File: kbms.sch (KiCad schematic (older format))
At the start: 4 parts

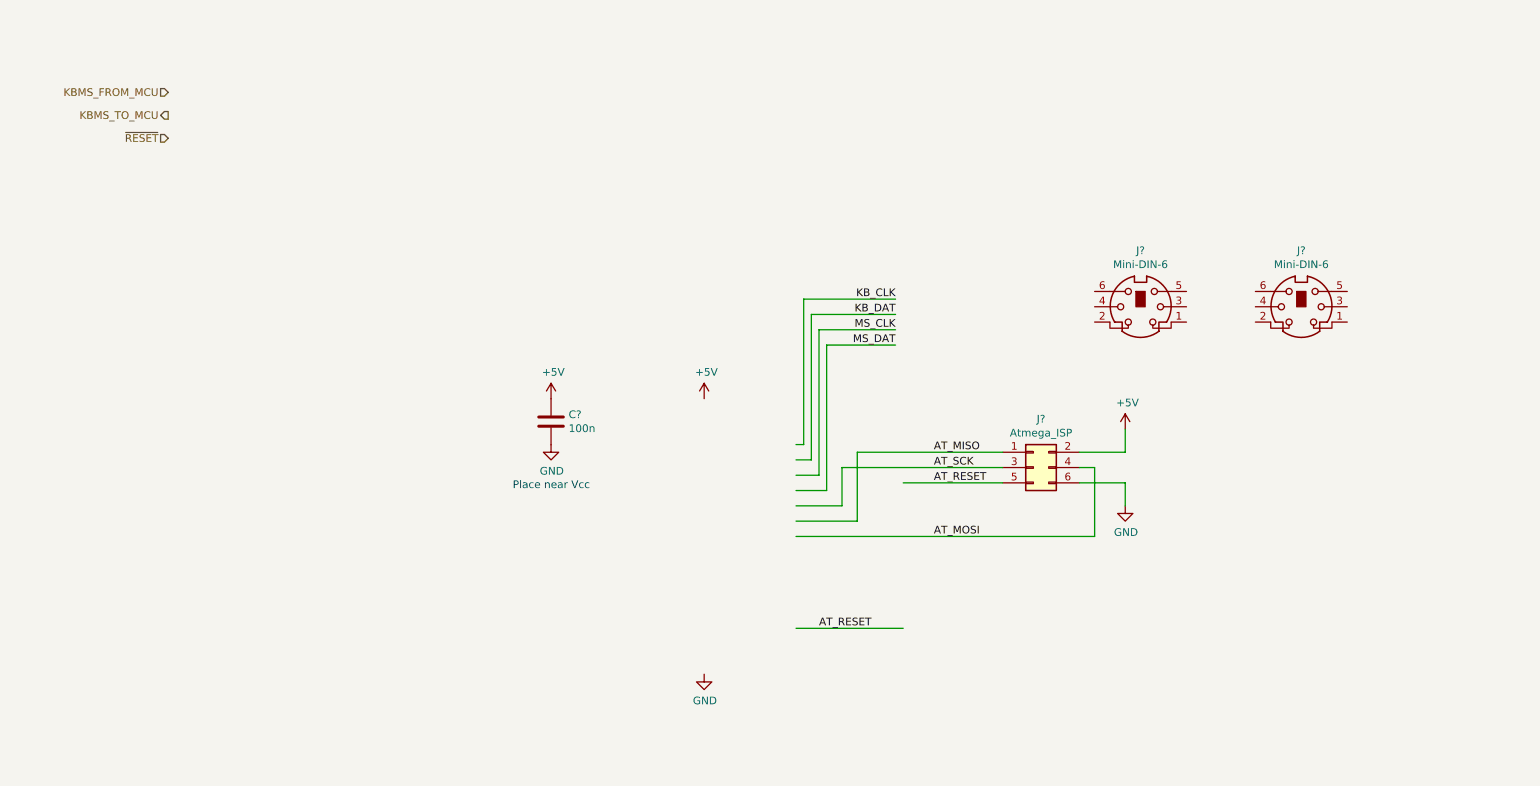
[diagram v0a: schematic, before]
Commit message: Added some footprints. Basic board outline.
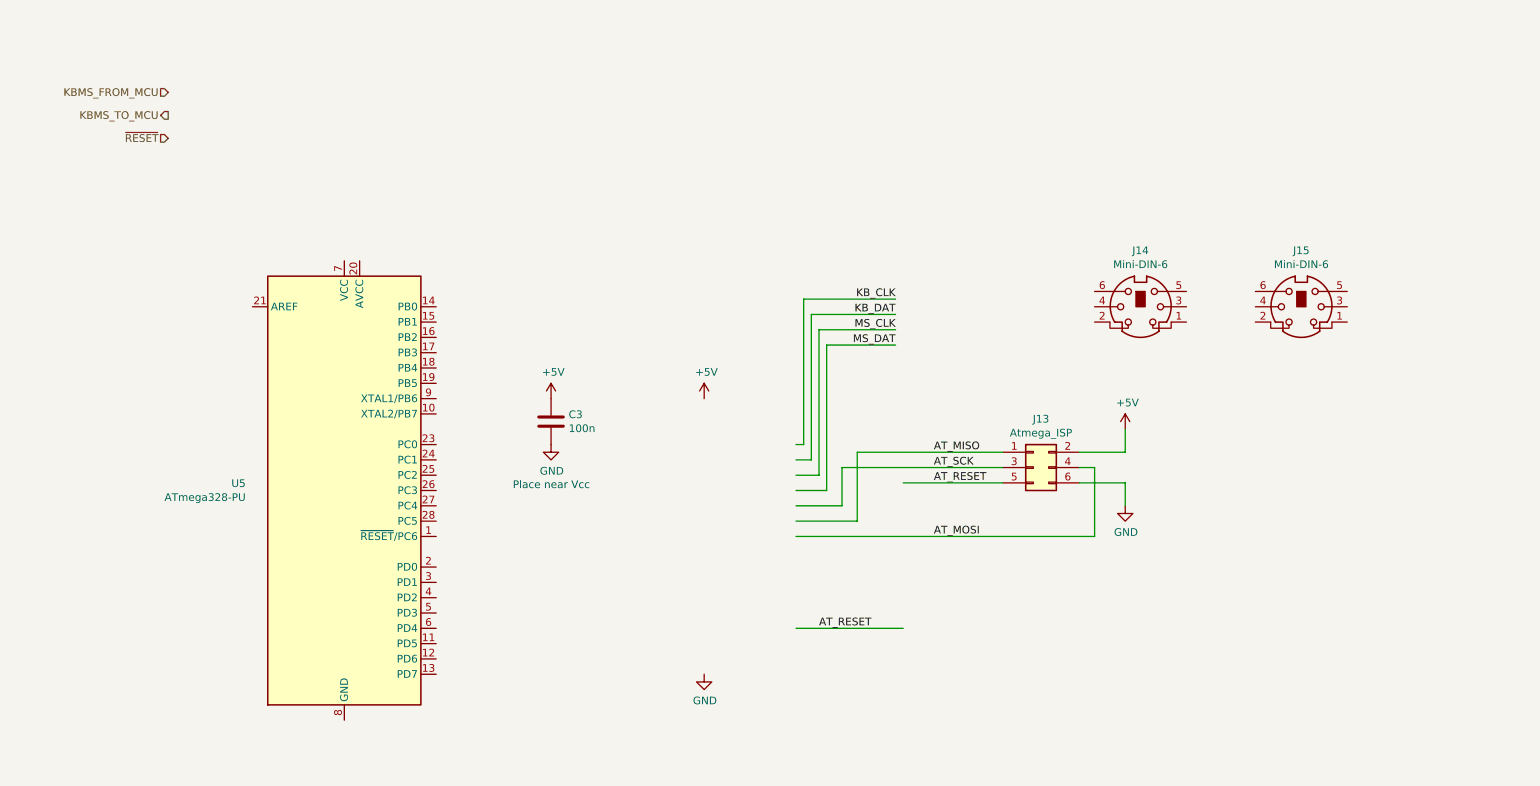
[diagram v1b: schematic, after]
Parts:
- added U5: ATmega328-PU, Package_DIP:DIP-28_W7.62mm, symbol MCU_Microchip_ATmega:ATmega328-PU
- C3: renamed from C?; footprint (none) -> Capacitor_THT:C_Disc_D5.0mm_W2.5mm_P2.50mm
- J13: renamed from J?; footprint (none) -> Connector_PinHeader_2.54mm:PinHeader_2x03_P2.54mm_Vertical
- J14, J15: renamed from J?; footprint (none) -> JGP Footprints:mini-DIN 6
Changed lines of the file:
@@
 $Descr A4 11693 8268
 encoding utf-8
-Sheet 11 11
+Sheet 9 11
 Title "Neotron 32K"
 Date "2019-12-08"
@@
 P 7350 3650
 AR Path="/5DF43D9A" Ref="J?"  Part="1"
-AR Path="/5DF2662E/5DF43D9A" Ref="J?"  Part="1"
-F 0 "J?" H 7400 3967 50  0000 C CNN
+AR Path="/5DF2662E/5DF43D9A" Ref="J13"  Part="1"
+F 0 "J13" H 7400 3967 50  0000 C CNN
 F 1 "Atmega_ISP" H 7400 3876 50  0000 C CNN
-F 2 "" H 7350 3650 50  0001 C CNN
+F 2 "Connector_PinHeader_2.54mm:PinHeader_2x03_P2.54mm_Vertical" H 7350 3650 50  0001 C CNN
 F 3 "~" H 7350 3650 50  0001 C CNN
 	1    7350 3650
@@
 P 7950 3400
 AR Path="/5DF43DA0" Ref="#PWR?"  Part="1"
-AR Path="/5DF2662E/5DF43DA0" Ref="#PWR0105"  Part="1"
-F 0 "#PWR0105" H 7950 3250 50  0001 C CNN
+AR Path="/5DF2662E/5DF43DA0" Ref="#PWR018"  Part="1"
+F 0 "#PWR018" H 7950 3250 50  0001 C CNN
 F 1 "+5V" H 7965 3573 50  0000 C CNN
 F 2 "" H 7950 3400 50  0001 C CNN
@@
 P 7950 3900
 AR Path="/5DF43DA6" Ref="#PWR?"  Part="1"
-AR Path="/5DF2662E/5DF43DA6" Ref="#PWR0106"  Part="1"
-F 0 "#PWR0106" H 7950 3650 50  0001 C CNN
+AR Path="/5DF2662E/5DF43DA6" Ref="#PWR019"  Part="1"
+F 0 "#PWR019" H 7950 3650 50  0001 C CNN
 F 1 "GND" H 7955 3727 50  0000 C CNN
 F 2 "" H 7950 3900 50  0001 C CNN
@@
 P 5200 3200
 AR Path="/5DF43DBB" Ref="#PWR?"  Part="1"
-AR Path="/5DF2662E/5DF43DBB" Ref="#PWR0107"  Part="1"
-F 0 "#PWR0107" H 5200 3050 50  0001 C CNN
+AR Path="/5DF2662E/5DF43DBB" Ref="#PWR016"  Part="1"
+F 0 "#PWR016" H 5200 3050 50  0001 C CNN
 F 1 "+5V" H 5215 3373 50  0000 C CNN
 F 2 "" H 5200 3200 50  0001 C CNN
@@
 P 5200 5000
 AR Path="/5DF43DC1" Ref="#PWR?"  Part="1"
-AR Path="/5DF2662E/5DF43DC1" Ref="#PWR0108"  Part="1"
-F 0 "#PWR0108" H 5200 4750 50  0001 C CNN
+AR Path="/5DF2662E/5DF43DC1" Ref="#PWR017"  Part="1"
+F 0 "#PWR017" H 5200 4750 50  0001 C CNN
 F 1 "GND" H 5205 4827 50  0000 C CNN
 F 2 "" H 5200 5000 50  0001 C CNN
@@
 P 4200 3350
 AR Path="/5DF43DC7" Ref="C?"  Part="1"
-AR Path="/5DF2662E/5DF43DC7" Ref="C?"  Part="1"
-F 0 "C?" H 4315 3396 50  0000 L CNN
+AR Path="/5DF2662E/5DF43DC7" Ref="C3"  Part="1"
+F 0 "C3" H 4315 3396 50  0000 L CNN
 F 1 "100n" H 4315 3305 50  0000 L CNN
-F 2 "" H 4238 3200 50  0001 C CNN
+F 2 "Capacitor_THT:C_Disc_D5.0mm_W2.5mm_P2.50mm" H 4238 3200 50  0001 C CNN
 F 3 "~" H 4200 3350 50  0001 C CNN
 	1    4200 3350
@@
 P 4200 3200
 AR Path="/5DF43DCD" Ref="#PWR?"  Part="1"
-AR Path="/5DF2662E/5DF43DCD" Ref="#PWR0109"  Part="1"
-F 0 "#PWR0109" H 4200 3050 50  0001 C CNN
+AR Path="/5DF2662E/5DF43DCD" Ref="#PWR014"  Part="1"
+F 0 "#PWR014" H 4200 3050 50  0001 C CNN
 F 1 "+5V" H 4215 3373 50  0000 C CNN
 F 2 "" H 4200 3200 50  0001 C CNN
@@
 P 4200 3500
 AR Path="/5DF43DD3" Ref="#PWR?"  Part="1"
-AR Path="/5DF2662E/5DF43DD3" Ref="#PWR0110"  Part="1"
-F 0 "#PWR0110" H 4200 3250 50  0001 C CNN
+AR Path="/5DF2662E/5DF43DD3" Ref="#PWR015"  Part="1"
+F 0 "#PWR015" H 4200 3250 50  0001 C CNN
 F 1 "GND" H 4205 3327 50  0000 C CNN
 F 2 "" H 4200 3500 50  0001 C CNN
@@
 P 8050 2600
 AR Path="/5DF4AE86" Ref="J?"  Part="1"
-AR Path="/5DF2662E/5DF4AE86" Ref="J?"  Part="1"
-F 0 "J?" H 8050 2967 50  0000 C CNN
+AR Path="/5DF2662E/5DF4AE86" Ref="J14"  Part="1"
+F 0 "J14" H 8050 2967 50  0000 C CNN
 F 1 "Mini-DIN-6" H 8050 2876 50  0000 C CNN
-F 2 "" H 8050 2600 50  0001 C CNN
+F 2 "JGP Footprints:mini-DIN 6" H 8050 2600 50  0001 C CNN
 F 3 "http://service.powerdynamics.com/ec/Catalog17/Section%2011.pdf" H 8050 2600 50  0001 C CNN
 	1    8050 2600
@@
 P 9100 2600
 AR Path="/5DF4AE8C" Ref="J?"  Part="1"
-AR Path="/5DF2662E/5DF4AE8C" Ref="J?"  Part="1"
-F 0 "J?" H 9100 2967 50  0000 C CNN
+AR Path="/5DF2662E/5DF4AE8C" Ref="J15"  Part="1"
+F 0 "J15" H 9100 2967 50  0000 C CNN
 F 1 "Mini-DIN-6" H 9100 2876 50  0000 C CNN
-F 2 "" H 9100 2600 50  0001 C CNN
+F 2 "JGP Footprints:mini-DIN 6" H 9100 2600 50  0001 C CNN
 F 3 "http://service.powerdynamics.com/ec/Catalog17/Section%2011.pdf" H 9100 2600 50  0001 C CNN
 	1    9100 2600
@@
 Text HLabel 1700 1500 0    50   Input ~ 0
 ~RESET
+$Comp
+L MCU_Microchip_ATmega:ATmega328-PU U5
+U 1 1 5E0F9E16
+P 2850 3800
+F 0 "U5" H 2206 3846 50  0000 R CNN
+F 1 "ATmega328-PU" H 2206 3755 50  0000 R CNN
+F 2 "Package_DIP:DIP-28_W7.62mm" H 2850 3800 50  0001 C CIN
+F 3 "http://ww1.microchip.com/downloads/en/DeviceDoc/ATmega328_P%20AVR%20MCU%20with%20picoPower%20Technology%20Data%20Sheet%2040001984A.pdf" H 2850 3800 50  0001 C CNN
+	1    2850 3800
+	1    0    0    -1
+$EndComp
 $EndSCHEMATC

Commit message: Completed Power, SD, MIDI, Parallel and Joystick sheets.
Switch to sheet based 100x part numbering.
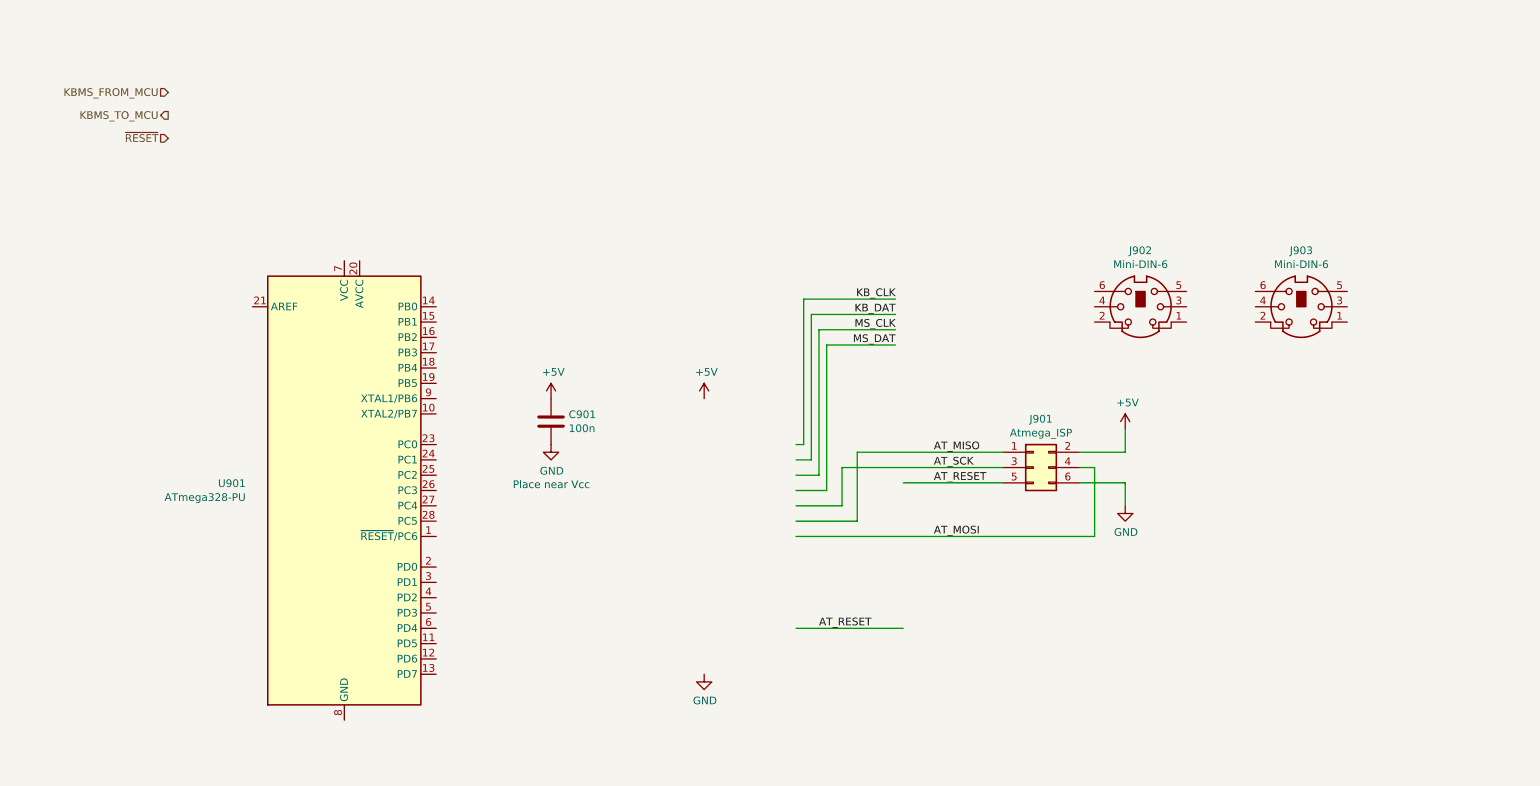
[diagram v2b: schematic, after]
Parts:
- renumbered C3 to C901, J13 to J901, J14 to J902, J15 to J903, U5 to U901
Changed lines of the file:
@@
 P 7350 3650
 AR Path="/5DF43D9A" Ref="J?"  Part="1"
-AR Path="/5DF2662E/5DF43D9A" Ref="J13"  Part="1"
-F 0 "J13" H 7400 3967 50  0000 C CNN
+AR Path="/5DF2662E/5DF43D9A" Ref="J901"  Part="1"
+F 0 "J901" H 7400 3967 50  0000 C CNN
 F 1 "Atmega_ISP" H 7400 3876 50  0000 C CNN
 F 2 "Connector_PinHeader_2.54mm:PinHeader_2x03_P2.54mm_Vertical" H 7350 3650 50  0001 C CNN
@@
 P 7950 3400
 AR Path="/5DF43DA0" Ref="#PWR?"  Part="1"
-AR Path="/5DF2662E/5DF43DA0" Ref="#PWR018"  Part="1"
-F 0 "#PWR018" H 7950 3250 50  0001 C CNN
+AR Path="/5DF2662E/5DF43DA0" Ref="#PWR0905"  Part="1"
+F 0 "#PWR0905" H 7950 3250 50  0001 C CNN
 F 1 "+5V" H 7965 3573 50  0000 C CNN
 F 2 "" H 7950 3400 50  0001 C CNN
@@
 P 7950 3900
 AR Path="/5DF43DA6" Ref="#PWR?"  Part="1"
-AR Path="/5DF2662E/5DF43DA6" Ref="#PWR019"  Part="1"
-F 0 "#PWR019" H 7950 3650 50  0001 C CNN
+AR Path="/5DF2662E/5DF43DA6" Ref="#PWR0906"  Part="1"
+F 0 "#PWR0906" H 7950 3650 50  0001 C CNN
 F 1 "GND" H 7955 3727 50  0000 C CNN
 F 2 "" H 7950 3900 50  0001 C CNN
@@
 P 5200 3200
 AR Path="/5DF43DBB" Ref="#PWR?"  Part="1"
-AR Path="/5DF2662E/5DF43DBB" Ref="#PWR016"  Part="1"
-F 0 "#PWR016" H 5200 3050 50  0001 C CNN
+AR Path="/5DF2662E/5DF43DBB" Ref="#PWR0903"  Part="1"
+F 0 "#PWR0903" H 5200 3050 50  0001 C CNN
 F 1 "+5V" H 5215 3373 50  0000 C CNN
 F 2 "" H 5200 3200 50  0001 C CNN
@@
 P 5200 5000
 AR Path="/5DF43DC1" Ref="#PWR?"  Part="1"
-AR Path="/5DF2662E/5DF43DC1" Ref="#PWR017"  Part="1"
-F 0 "#PWR017" H 5200 4750 50  0001 C CNN
+AR Path="/5DF2662E/5DF43DC1" Ref="#PWR0904"  Part="1"
+F 0 "#PWR0904" H 5200 4750 50  0001 C CNN
 F 1 "GND" H 5205 4827 50  0000 C CNN
 F 2 "" H 5200 5000 50  0001 C CNN
@@
 P 4200 3350
 AR Path="/5DF43DC7" Ref="C?"  Part="1"
-AR Path="/5DF2662E/5DF43DC7" Ref="C3"  Part="1"
-F 0 "C3" H 4315 3396 50  0000 L CNN
+AR Path="/5DF2662E/5DF43DC7" Ref="C901"  Part="1"
+F 0 "C901" H 4315 3396 50  0000 L CNN
 F 1 "100n" H 4315 3305 50  0000 L CNN
 F 2 "Capacitor_THT:C_Disc_D5.0mm_W2.5mm_P2.50mm" H 4238 3200 50  0001 C CNN
@@
 P 4200 3200
 AR Path="/5DF43DCD" Ref="#PWR?"  Part="1"
-AR Path="/5DF2662E/5DF43DCD" Ref="#PWR014"  Part="1"
-F 0 "#PWR014" H 4200 3050 50  0001 C CNN
+AR Path="/5DF2662E/5DF43DCD" Ref="#PWR0901"  Part="1"
+F 0 "#PWR0901" H 4200 3050 50  0001 C CNN
 F 1 "+5V" H 4215 3373 50  0000 C CNN
 F 2 "" H 4200 3200 50  0001 C CNN
@@
 P 4200 3500
 AR Path="/5DF43DD3" Ref="#PWR?"  Part="1"
-AR Path="/5DF2662E/5DF43DD3" Ref="#PWR015"  Part="1"
-F 0 "#PWR015" H 4200 3250 50  0001 C CNN
+AR Path="/5DF2662E/5DF43DD3" Ref="#PWR0902"  Part="1"
+F 0 "#PWR0902" H 4200 3250 50  0001 C CNN
 F 1 "GND" H 4205 3327 50  0000 C CNN
 F 2 "" H 4200 3500 50  0001 C CNN
@@
 P 8050 2600
 AR Path="/5DF4AE86" Ref="J?"  Part="1"
-AR Path="/5DF2662E/5DF4AE86" Ref="J14"  Part="1"
-F 0 "J14" H 8050 2967 50  0000 C CNN
+AR Path="/5DF2662E/5DF4AE86" Ref="J902"  Part="1"
+F 0 "J902" H 8050 2967 50  0000 C CNN
 F 1 "Mini-DIN-6" H 8050 2876 50  0000 C CNN
 F 2 "JGP Footprints:mini-DIN 6" H 8050 2600 50  0001 C CNN
@@
 P 9100 2600
 AR Path="/5DF4AE8C" Ref="J?"  Part="1"
-AR Path="/5DF2662E/5DF4AE8C" Ref="J15"  Part="1"
-F 0 "J15" H 9100 2967 50  0000 C CNN
+AR Path="/5DF2662E/5DF4AE8C" Ref="J903"  Part="1"
+F 0 "J903" H 9100 2967 50  0000 C CNN
 F 1 "Mini-DIN-6" H 9100 2876 50  0000 C CNN
 F 2 "JGP Footprints:mini-DIN 6" H 9100 2600 50  0001 C CNN
@@
 ~RESET
 $Comp
-L MCU_Microchip_ATmega:ATmega328-PU U5
+L MCU_Microchip_ATmega:ATmega328-PU U901
 U 1 1 5E0F9E16
 P 2850 3800
-F 0 "U5" H 2206 3846 50  0000 R CNN
+F 0 "U901" H 2206 3846 50  0000 R CNN
 F 1 "ATmega328-PU" H 2206 3755 50  0000 R CNN
 F 2 "Package_DIP:DIP-28_W7.62mm" H 2850 3800 50  0001 C CIN

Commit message: Schematic capture draft complete.
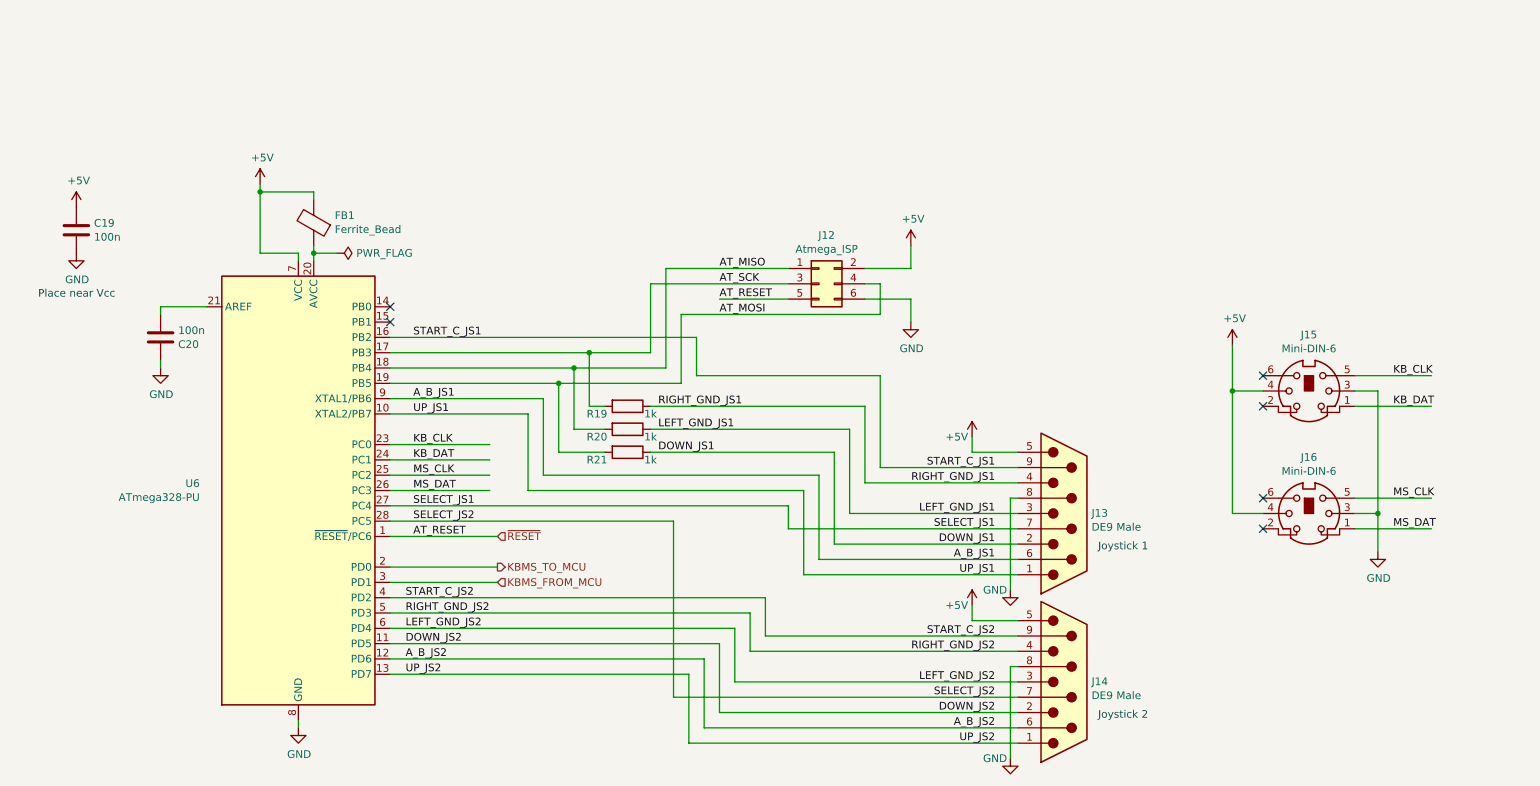
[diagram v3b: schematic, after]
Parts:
- added C20: 100n, Capacitor_THT:C_Disc_D3.0mm_W2.0mm_P2.50mm, symbol Device:C
- added FB1: Ferrite_Bead, symbol Device:Ferrite_Bead
- added J13, J14: DE9 Male, Connector_Dsub:DSUB-9_Female_Horizontal_P2.77x2.84mm_EdgePinOffset4.94mm_Housed_MountingHolesOffset7.48mm, symbol Connector:DB9_Male
- added R19, R20, R21: 1k, symbol Device:R
- C19: renamed from C901; footprint Capacitor_THT:C_Disc_D5.0mm_W2.5mm_P2.50mm -> Capacitor_THT:C_Disc_D3.0mm_W2.0mm_P2.50mm
- renumbered J901 to J12, J902 to J15, J903 to J16, U901 to U6
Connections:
- net labels added: A_B_JS1, A_B_JS2, DOWN_JS1, DOWN_JS2, LEFT_GND_JS1, LEFT_GND_JS2, RIGHT_GND_JS1, RIGHT_GND_JS2, SELECT_JS1, SELECT_JS2, START_C_JS1, START_C_JS2, UP_JS1, UP_JS2
- wire segments 27 -> 113
- no-connect marks 0 -> 6
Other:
- note added: "Joystick 1"
- note added: "Joystick 2"
- moved on the sheet: C19, J12, J15, J16, U6

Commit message: Tidied up Atmega power. Added page titles.
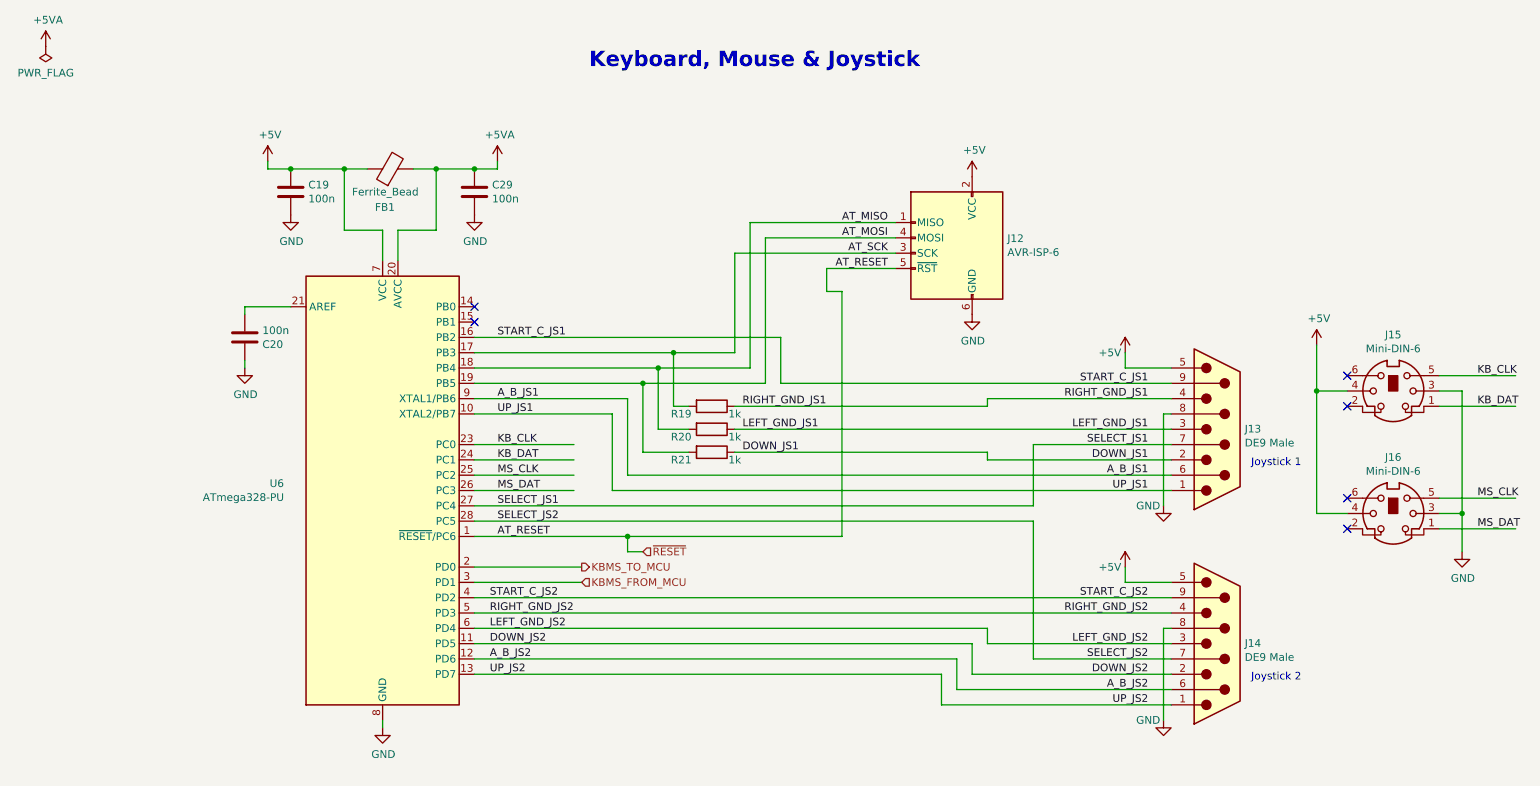
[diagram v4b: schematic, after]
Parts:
- removed J12: Atmega_ISP, Connector_PinHeader_2.54mm:PinHeader_2x03_P2.54mm_Vertical, symbol Connector_Generic:Conn_02x03_Odd_Even
- added C29: 100n, Capacitor_THT:C_Disc_D3.0mm_W2.0mm_P2.50mm, symbol Device:C
- added J12: AVR-ISP-6, symbol Connector:AVR-ISP-6
- FB1: footprint (none) -> Inductor_THT:L_Axial_L12.8mm_D5.8mm_P5.08mm_Vertical_Fastron_HBCC; Digikey (none) -> 535-12742-ND
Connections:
- net labels added: +5VA
- wire segments 113 -> 106
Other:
- note added: "Keyboard, Mouse & Joystick"
- note removed: "Place near Vcc"
- moved on the sheet: C19, C20, FB1, J13, J14, J15, J16, R19, R20, R21, U6
